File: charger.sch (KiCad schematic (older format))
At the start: 8 parts, among them U4 MCP73831

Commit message: Fixed NTLJF3117P MOSFET pin layout
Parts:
- removed C5: 10u, Capacitors_Tantalum_SMD:CP_Tantalum_Case-A_EIA-3216-18_Reflow, symbol CP
- added C5: 10u, Capacitors_SMD:C_0805, symbol C
- D1: value LED -> Red LED
- D2: value LED -> Green LED
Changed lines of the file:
@@
 P 4050 3800
 F 0 "D1" H 4042 3545 50  0000 C CNN
-F 1 "LED" H 4042 3636 50  0000 C CNN
+F 1 "Red LED" H 4042 3636 50  0000 C CNN
 F 2 "LEDs:LED_0805" H 4042 3636 50  0001 C CNN
 F 3 "" H 4050 3800 50  0000 C CNN
@@
 F 3 "" H 2850 3600 50  0000 C CNN
 	1    2850 3600
-	1    0    0    -1
-$EndComp
-$Comp
-L CP C5
-U 1 1 58AA53C6
-P 6700 3400
-F 0 "C5" H 6818 3446 50  0000 L CNN
-F 1 "10u" H 6818 3355 50  0000 L CNN
-F 2 "Capacitors_Tantalum_SMD:CP_Tantalum_Case-A_EIA-3216-18_Reflow" H 6818 3355 50  0001 L CNN
-F 3 "" H 6700 3400 50  0000 C CNN
-F 4 "AVX" H 6700 3400 60  0001 C CNN "MFN"
-F 5 "TAJA106K016TNJ" H 6700 3400 60  0001 C CNN "MFP"
-	1    6700 3400
 	1    0    0    -1
 $EndComp
@@
 P 4050 4300
 F 0 "D2" H 4042 4045 50  0000 C CNN
-F 1 "LED" H 4042 4136 50  0000 C CNN
+F 1 "Green LED" H 4042 4136 50  0000 C CNN
 F 2 "LEDs:LED_0805" H 4042 4136 50  0001 C CNN
 F 3 "" H 4050 4300 50  0000 C CNN
@@
 Wire Wire Line
 	4050 3950 4050 4150
+$Comp
+L C C5
+U 1 1 59F7E223
+P 6700 3400
+F 0 "C5" H 6815 3446 50  0000 L CNN
+F 1 "10u" H 6815 3355 50  0000 L CNN
+F 2 "Capacitors_SMD:C_0805" H 6815 3309 50  0001 L CNN
+F 3 "" H 6700 3400 50  0000 C CNN
+F 4 "Murata" H 6700 3400 60  0001 C CNN "MFN"
+F 5 "GRM21BR61E106KA73L" H 6700 3400 60  0001 C CNN "MFP"
+	1    6700 3400
+	1    0    0    -1
+$EndComp
 $EndSCHEMATC

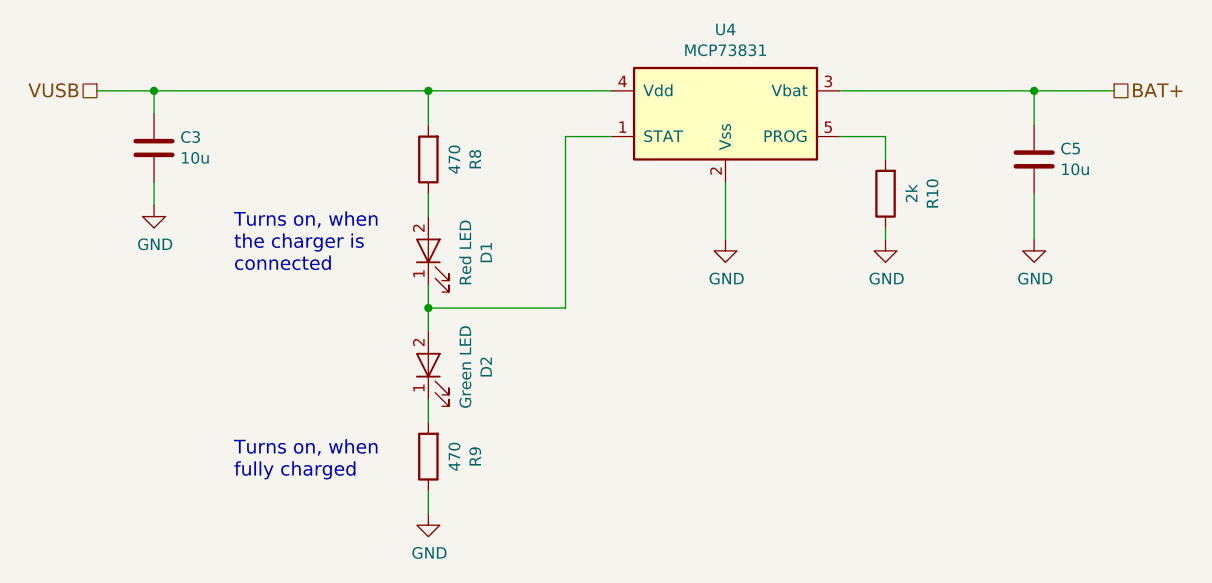
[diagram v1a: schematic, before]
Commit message: Moved MCU pins around to make sure that they do not interfere with the programmer Moved ISP Header closer to the edge of the board to allow easier access with the programmer Added pulldown resistor to the DCD/DC converters enable pin to make sure it stays off in case of failure Added more PDFs of components
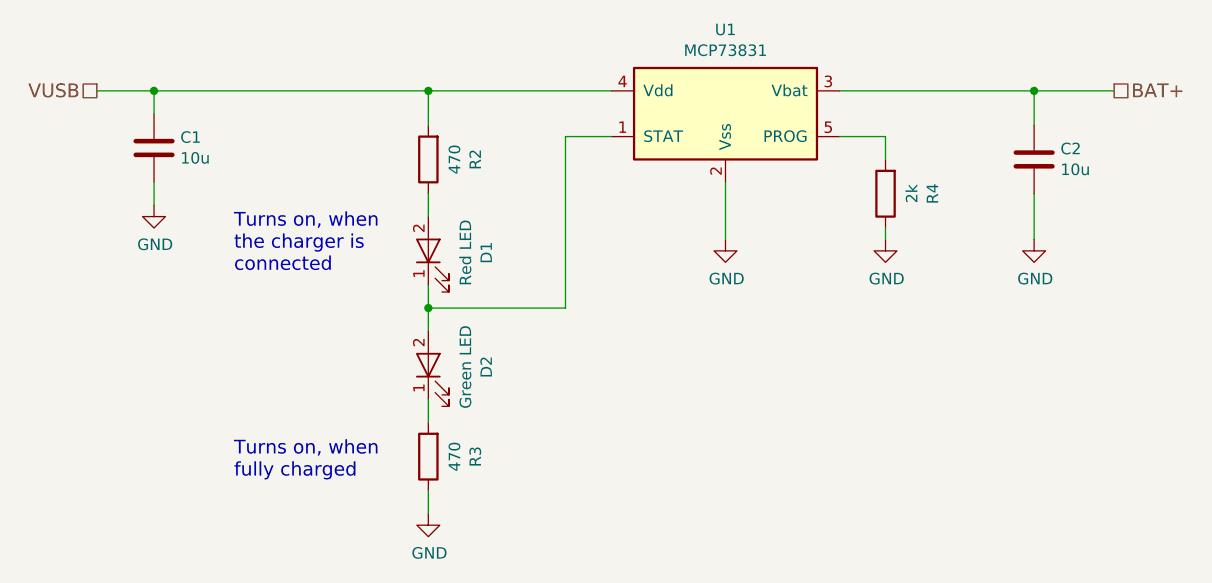
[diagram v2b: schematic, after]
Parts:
- renumbered C3 to C1, C5 to C2, R8 to R2, R9 to R3, R10 to R4, U4 to U1
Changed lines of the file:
@@
 VUSB
 $Comp
-L R R8
+L R R2
 U 1 1 58AA539F
 P 4050 3400
-F 0 "R8" V 3843 3400 50  0000 C CNN
+F 0 "R2" V 3843 3400 50  0000 C CNN
 F 1 "470" V 3934 3400 50  0000 C CNN
 F 2 "Resistors_SMD:R_0603" V 3935 3400 50  0001 C CNN
@@
 BAT+
 $Comp
-L C C3
+L C C1
 U 1 1 58AA53B1
 P 2850 3350
-F 0 "C3" H 2965 3396 50  0000 L CNN
+F 0 "C1" H 2965 3396 50  0000 L CNN
 F 1 "10u" H 2965 3305 50  0000 L CNN
 F 2 "Capacitors_SMD:C_0805" H 2965 3259 50  0001 L CNN
@@
 $EndComp
 $Comp
-L MCP73831 U4
+L MCP73831 U1
 U 1 1 58AA53DC
 P 5350 3200
-F 0 "U4" H 5350 3567 50  0000 C CNN
+F 0 "U1" H 5350 3567 50  0000 C CNN
 F 1 "MCP73831" H 5350 3476 50  0000 C CNN
 F 2 "TO_SOT_Packages_SMD:SOT-23-5" H 5350 3476 50  0001 C CNN
@@
 $EndComp
 $Comp
-L R R10
+L R R4
 U 1 1 58AA53EC
 P 6050 3550
-F 0 "R10" V 5843 3550 50  0000 C CNN
+F 0 "R4" V 5843 3550 50  0000 C CNN
 F 1 "2k" V 5934 3550 50  0000 C CNN
 F 2 "Resistors_SMD:R_0603" V 5935 3550 50  0001 C CNN
@@
 $EndComp
 $Comp
-L R R9
+L R R3
 U 1 1 58AA6815
 P 4050 4700
-F 0 "R9" V 3843 4700 50  0000 C CNN
+F 0 "R3" V 3843 4700 50  0000 C CNN
 F 1 "470" V 3934 4700 50  0000 C CNN
 F 2 "Resistors_SMD:R_0603" V 3935 4700 50  0001 C CNN
@@
 	4050 3950 4050 4150
 $Comp
-L C C5
+L C C2
 U 1 1 59F7E223
 P 6700 3400
-F 0 "C5" H 6815 3446 50  0000 L CNN
+F 0 "C2" H 6815 3446 50  0000 L CNN
 F 1 "10u" H 6815 3355 50  0000 L CNN
 F 2 "Capacitors_SMD:C_0805" H 6815 3309 50  0001 L CNN

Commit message: Added part names and BOM Added Gerber files
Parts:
- D1: MFN (none) -> Kingbright; MFP (none) -> AP2012SRCPRV
- R2, R3: MFN Vishay -> Yageo; MFP CRCW0603470RFKEA -> RC0603FR-07470RL
- R4: MFN Vishay -> Yageo; MFP CRCW06032K00FKEA -> RC0603FR-072KL
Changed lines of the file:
@@
 F 2 "Resistors_SMD:R_0603" V 3935 3400 50  0001 C CNN
 F 3 "" H 4050 3400 50  0000 C CNN
-F 4 "Vishay" H 4050 3400 60  0001 C CNN "MFN"
-F 5 "CRCW0603470RFKEA" H 4050 3400 60  0001 C CNN "MFP"
+F 4 "Yageo" H 4050 3400 60  0001 C CNN "MFN"
+F 5 "RC0603FR-07470RL" H 4050 3400 60  0001 C CNN "MFP"
 	1    4050 3400
 	-1   0    0    1
@@
 F 2 "LEDs:LED_0805" H 4042 3636 50  0001 C CNN
 F 3 "" H 4050 3800 50  0000 C CNN
-F 4 "Red LED" H 4050 3800 60  0001 C CNN "Note"
+F 4 "Kingbright" H 4050 3800 60  0001 C CNN "MFN"
+F 5 "AP2012SRCPRV" H 4050 3800 60  0001 C CNN "MFP"
+F 6 "Red LED" H 4050 3800 60  0001 C CNN "Note"
 	1    4050 3800
 	0    -1   -1   0
@@
 F 2 "Resistors_SMD:R_0603" V 5935 3550 50  0001 C CNN
 F 3 "" H 6050 3550 50  0000 C CNN
-F 4 "Vishay" H 6050 3550 60  0001 C CNN "MFN"
-F 5 "CRCW06032K00FKEA" H 6050 3550 60  0001 C CNN "MFP"
+F 4 "Yageo" H 6050 3550 60  0001 C CNN "MFN"
+F 5 "RC0603FR-072KL" H 6050 3550 60  0001 C CNN "MFP"
 	1    6050 3550
 	-1   0    0    1
@@
 F 2 "Resistors_SMD:R_0603" V 3935 4700 50  0001 C CNN
 F 3 "" H 4050 4700 50  0000 C CNN
-F 4 "Vishay" H 4050 4700 60  0001 C CNN "MFN"
-F 5 "CRCW0603470RFKEA" H 4050 4700 60  0001 C CNN "MFP"
+F 4 "Yageo" H 4050 4700 60  0001 C CNN "MFN"
+F 5 "RC0603FR-07470RL" H 4050 4700 60  0001 C CNN "MFP"
 	1    4050 4700
 	-1   0    0    1

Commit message: Preparing for v1.2 Updated to KiCAD 5 nightly Added resistors to isolate the programming pins Added transistor to drive the LED Replaced LTC3458 boost converter with an LTC3536 buck-boost converter to step down the USB power supply Added debugging jumper to test the voltage regulator
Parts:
- C1, C2: symbol C -> device:C
- D1, D2: symbol LED -> device:LED
- R2, R3, R4: symbol R -> device:R
- U1: symbol MCP73831 -> Microchip:MCP73831
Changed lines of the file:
@@
-EESchema Schematic File Version 2
-LIBS:power
-LIBS:device
-LIBS:transistors
-LIBS:conn
-LIBS:linear
-LIBS:regul
-LIBS:74xx
-LIBS:cmos4000
-LIBS:adc-dac
-LIBS:memory
-LIBS:xilinx
-LIBS:microcontrollers
-LIBS:dsp
-LIBS:microchip
-LIBS:analog_switches
-LIBS:motorola
-LIBS:texas
-LIBS:intel
-LIBS:audio
-LIBS:interface
-LIBS:digital-audio
-LIBS:philips
-LIBS:display
-LIBS:cypress
-LIBS:siliconi
-LIBS:opto
-LIBS:atmel
-LIBS:contrib
-LIBS:valves
-LIBS:switches
-LIBS:Microchip
-LIBS:On Semiconductor
-LIBS:Linear Technology
+EESchema Schematic File Version 4
 LIBS:main-cache
 EELAYER 26 0
@@
 VUSB
 $Comp
-L R R2
+L device:R R2
 U 1 1 58AA539F
 P 4050 3400
@@
 $EndComp
 $Comp
-L LED D1
+L device:LED D1
 U 1 1 58AA53A7
 P 4050 3800
@@
 BAT+
 $Comp
-L C C1
+L device:C C1
 U 1 1 58AA53B1
 P 2850 3350
@@
 $EndComp
 $Comp
-L GND #PWR04
+L power:GND #PWR06
 U 1 1 58AA53B8
 P 5350 3750
-F 0 "#PWR04" H 5350 3500 50  0001 C CNN
+F 0 "#PWR06" H 5350 3500 50  0001 C CNN
 F 1 "GND" H 5355 3577 50  0000 C CNN
 F 2 "" H 5350 3750 50  0000 C CNN
@@
 $EndComp
 $Comp
-L GND #PWR05
+L power:GND #PWR04
 U 1 1 58AA53BE
 P 2850 3600
-F 0 "#PWR05" H 2850 3350 50  0001 C CNN
+F 0 "#PWR04" H 2850 3350 50  0001 C CNN
 F 1 "GND" H 2855 3427 50  0000 C CNN
 F 2 "" H 2850 3600 50  0000 C CNN
@@
 $EndComp
 $Comp
-L GND #PWR06
+L power:GND #PWR08
 U 1 1 58AA53CD
 P 6700 3750
-F 0 "#PWR06" H 6700 3500 50  0001 C CNN
+F 0 "#PWR08" H 6700 3500 50  0001 C CNN
 F 1 "GND" H 6705 3577 50  0000 C CNN
 F 2 "" H 6700 3750 50  0000 C CNN
@@
 $EndComp
 $Comp
-L MCP73831 U1
+L Microchip:MCP73831 U1
 U 1 1 58AA53DC
 P 5350 3200
@@
 $EndComp
 $Comp
-L R R4
+L device:R R4
 U 1 1 58AA53EC
 P 6050 3550
@@
 $EndComp
 $Comp
-L GND #PWR07
+L power:GND #PWR07
 U 1 1 58AA53F5
 P 6050 3750
@@
 $EndComp
 $Comp
-L R R3
+L device:R R3
 U 1 1 58AA6815
 P 4050 4700
@@
 $EndComp
 $Comp
-L LED D2
+L device:LED D2
 U 1 1 58AA686B
 P 4050 4300
@@
 $EndComp
 $Comp
-L GND #PWR08
+L power:GND #PWR05
 U 1 1 58AA691B
 P 4050 4950
-F 0 "#PWR08" H 4050 4700 50  0001 C CNN
+F 0 "#PWR05" H 4050 4700 50  0001 C CNN
 F 1 "GND" H 4055 4777 50  0000 C CNN
 F 2 "" H 4050 4950 50  0000 C CNN
@@
 Turns on, when\nthe charger is\nconnected
 Wire Wire Line
-	2600 3100 4850 3100
+	2600 3100 2850 3100
 Wire Wire Line
 	2850 3100 2850 3200
@@
 	6050 3750 6050 3700
 Wire Wire Line
-	5850 3100 7050 3100
+	5850 3100 6700 3100
 Wire Wire Line
 	6700 3250 6700 3100
@@
 	4050 4050 4650 4050
 Wire Wire Line
-	4050 3950 4050 4150
-$Comp
-L C C2
+	4050 3950 4050 4050
+$Comp
+L device:C C2
 U 1 1 59F7E223
 P 6700 3400
@@
 	1    0    0    -1
 $EndComp
+Wire Wire Line
+	2850 3100 4050 3100
+Wire Wire Line
+	4050 3100 4850 3100
+Wire Wire Line
+	6700 3100 7050 3100
+Wire Wire Line
+	4050 4050 4050 4150
 $EndSCHEMATC

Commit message: Updated to Kicad v5.0
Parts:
- C1, C2: symbol device:C -> Device:C
- D1, D2: symbol device:LED -> Device:LED
- R2, R4: symbol device:R -> Device:R
- R3: value 470 -> 1k; symbol device:R -> Device:R; MFP RC0603FR-07470RL -> RC0603FR-071KL
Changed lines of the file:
@@
 VUSB
 $Comp
-L device:R R2
+L Device:R R2
 U 1 1 58AA539F
 P 4050 3400
@@
 $EndComp
 $Comp
-L device:LED D1
+L Device:LED D1
 U 1 1 58AA53A7
 P 4050 3800
@@
 BAT+
 $Comp
-L device:C C1
+L Device:C C1
 U 1 1 58AA53B1
 P 2850 3350
@@
 $EndComp
 $Comp
-L device:R R4
+L Device:R R4
 U 1 1 58AA53EC
 P 6050 3550
@@
 $EndComp
 $Comp
-L device:R R3
+L Device:R R3
 U 1 1 58AA6815
 P 4050 4700
 F 0 "R3" V 3843 4700 50  0000 C CNN
-F 1 "470" V 3934 4700 50  0000 C CNN
+F 1 "1k" V 3934 4700 50  0000 C CNN
 F 2 "Resistors_SMD:R_0603" V 3935 4700 50  0001 C CNN
 F 3 "" H 4050 4700 50  0000 C CNN
 F 4 "Yageo" H 4050 4700 60  0001 C CNN "MFN"
-F 5 "RC0603FR-07470RL" H 4050 4700 60  0001 C CNN "MFP"
+F 5 "RC0603FR-071KL" H 4050 4700 60  0001 C CNN "MFP"
 	1    4050 4700
 	-1   0    0    1
 $EndComp
 $Comp
-L device:LED D2
+L Device:LED D2
 U 1 1 58AA686B
 P 4050 4300
@@
 	4050 3950 4050 4050
 $Comp
-L device:C C2
+L Device:C C2
 U 1 1 59F7E223
 P 6700 3400

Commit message: Added power on state LED Updated to KiCAD 5.0
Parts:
- C1, C2: footprint Capacitors_SMD:C_0805 -> Capacitor_SMD:C_0805_2012Metric
- D1, D2: footprint LEDs:LED_0805 -> LED_SMD:LED_0805_2012Metric
- R2, R3, R4: footprint Resistors_SMD:R_0603 -> Resistor_SMD:R_0603_1608Metric
- U1: footprint TO_SOT_Packages_SMD:SOT-23-5 -> Package_TO_SOT_SMD:SOT-23-5
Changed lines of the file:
@@
 F 0 "R2" V 3843 3400 50  0000 C CNN
 F 1 "470" V 3934 3400 50  0000 C CNN
-F 2 "Resistors_SMD:R_0603" V 3935 3400 50  0001 C CNN
+F 2 "Resistor_SMD:R_0603_1608Metric" V 3935 3400 50  0001 C CNN
 F 3 "" H 4050 3400 50  0000 C CNN
 F 4 "Yageo" H 4050 3400 60  0001 C CNN "MFN"
@@
 F 0 "D1" H 4042 3545 50  0000 C CNN
 F 1 "Red LED" H 4042 3636 50  0000 C CNN
-F 2 "LEDs:LED_0805" H 4042 3636 50  0001 C CNN
+F 2 "LED_SMD:LED_0805_2012Metric" H 4042 3636 50  0001 C CNN
 F 3 "" H 4050 3800 50  0000 C CNN
 F 4 "Kingbright" H 4050 3800 60  0001 C CNN "MFN"
@@
 F 0 "C1" H 2965 3396 50  0000 L CNN
 F 1 "10u" H 2965 3305 50  0000 L CNN
-F 2 "Capacitors_SMD:C_0805" H 2965 3259 50  0001 L CNN
+F 2 "Capacitor_SMD:C_0805_2012Metric" H 2965 3259 50  0001 L CNN
 F 3 "" H 2850 3350 50  0000 C CNN
 F 4 "Murata" H 2850 3350 60  0001 C CNN "MFN"
@@
 F 0 "U1" H 5350 3567 50  0000 C CNN
 F 1 "MCP73831" H 5350 3476 50  0000 C CNN
-F 2 "TO_SOT_Packages_SMD:SOT-23-5" H 5350 3476 50  0001 C CNN
+F 2 "Package_TO_SOT_SMD:SOT-23-5" H 5350 3476 50  0001 C CNN
 F 3 "" H 4450 3600 50  0000 C CNN
 F 4 "Microchip" H 5350 3200 60  0001 C CNN "MFN"
@@
 F 0 "R4" V 5843 3550 50  0000 C CNN
 F 1 "2k" V 5934 3550 50  0000 C CNN
-F 2 "Resistors_SMD:R_0603" V 5935 3550 50  0001 C CNN
+F 2 "Resistor_SMD:R_0603_1608Metric" V 5935 3550 50  0001 C CNN
 F 3 "" H 6050 3550 50  0000 C CNN
 F 4 "Yageo" H 6050 3550 60  0001 C CNN "MFN"
@@
 F 0 "R3" V 3843 4700 50  0000 C CNN
 F 1 "1k" V 3934 4700 50  0000 C CNN
-F 2 "Resistors_SMD:R_0603" V 3935 4700 50  0001 C CNN
+F 2 "Resistor_SMD:R_0603_1608Metric" V 3935 4700 50  0001 C CNN
 F 3 "" H 4050 4700 50  0000 C CNN
 F 4 "Yageo" H 4050 4700 60  0001 C CNN "MFN"
@@
 F 0 "D2" H 4042 4045 50  0000 C CNN
 F 1 "Green LED" H 4042 4136 50  0000 C CNN
-F 2 "LEDs:LED_0805" H 4042 4136 50  0001 C CNN
+F 2 "LED_SMD:LED_0805_2012Metric" H 4042 4136 50  0001 C CNN
 F 3 "" H 4050 4300 50  0000 C CNN
 F 4 "Green LED" H 4050 4300 60  0001 C CNN "Note"
@@
 F 0 "C2" H 6815 3446 50  0000 L CNN
 F 1 "10u" H 6815 3355 50  0000 L CNN
-F 2 "Capacitors_SMD:C_0805" H 6815 3309 50  0001 L CNN
+F 2 "Capacitor_SMD:C_0805_2012Metric" H 6815 3309 50  0001 L CNN
 F 3 "" H 6700 3400 50  0000 C CNN
 F 4 "Murata" H 6700 3400 60  0001 C CNN "MFN"

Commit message: Added part numbers Updated BOM
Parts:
- D2: MFN (none) -> Kingbright; MFP (none) -> AP2012SGD3
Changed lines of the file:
@@
 F 2 "LED_SMD:LED_0805_2012Metric" H 4042 4136 50  0001 C CNN
 F 3 "" H 4050 4300 50  0000 C CNN
-F 4 "Green LED" H 4050 4300 60  0001 C CNN "Note"
+F 4 "Kingbright" H 4050 4300 50  0001 C CNN "MFN"
+F 5 "AP2012SGD3" H 4050 4300 50  0001 C CNN "MFP"
+F 6 "Green LED" H 4050 4300 60  0001 C CNN "Note"
 	1    4050 4300
 	0    -1   -1   0
